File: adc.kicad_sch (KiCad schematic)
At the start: 13 parts, among them U4 PCM1860DBT, U5 STM32F401CDUx, Y1 _ MHz

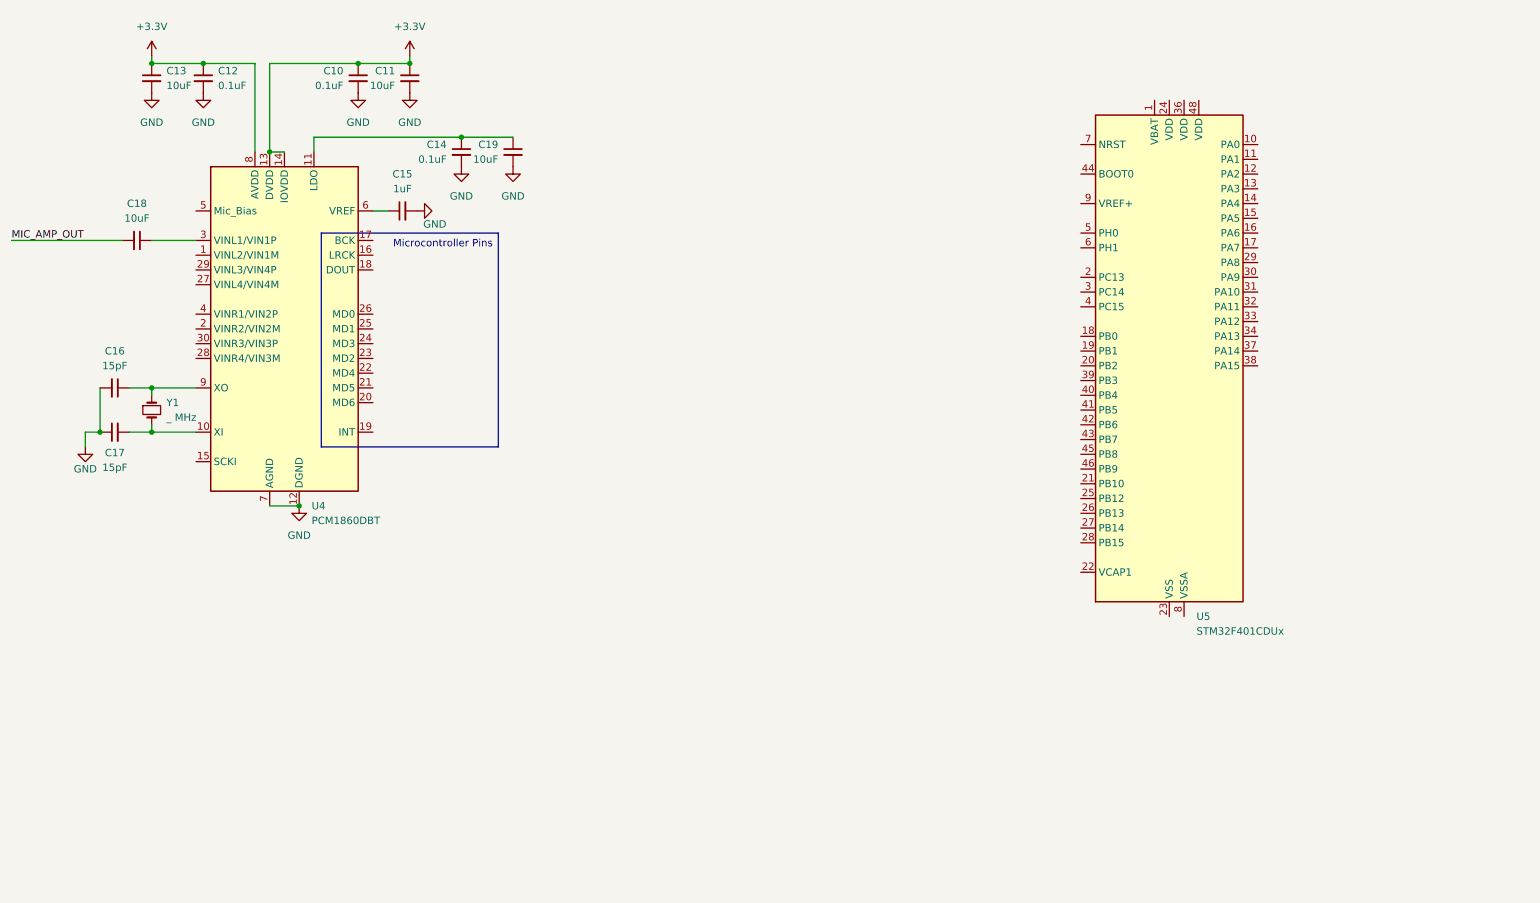
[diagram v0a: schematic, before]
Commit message: implementing full adc and semi-microcontroller
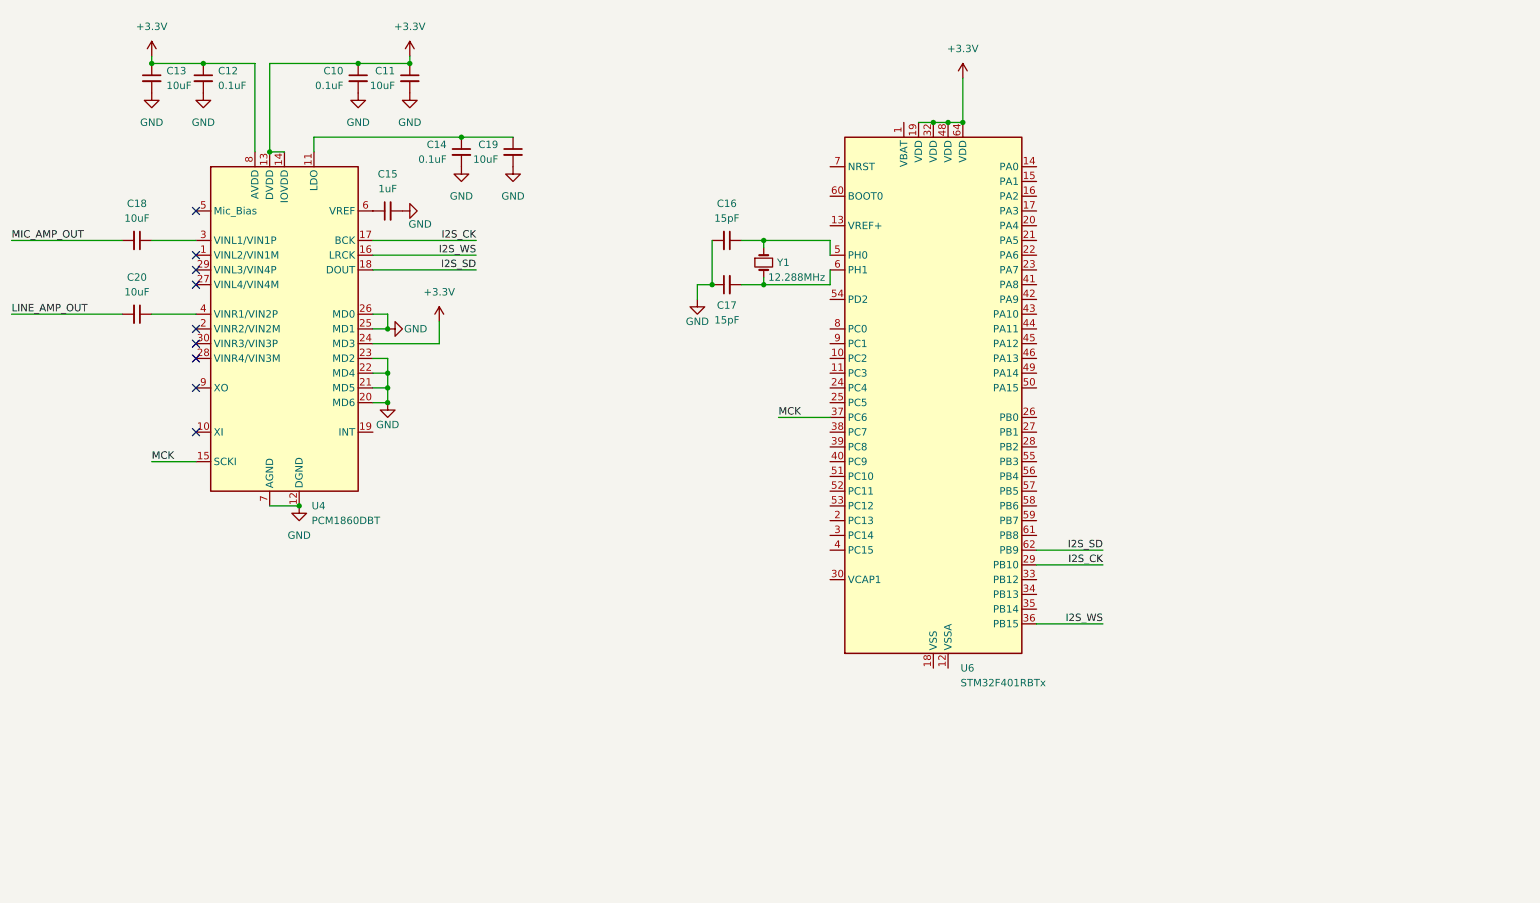
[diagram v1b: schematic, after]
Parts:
- removed U5: STM32F401CDUx, Package_DFN_QFN:QFN-48-1EP_7x7mm_P0.5mm_EP5.6x5.6mm, symbol MCU_ST_STM32F4:STM32F401CDUx
- added C20: 10uF, symbol Device:C_Small
- added U6: STM32F401RBTx, Package_QFP:LQFP-64_10x10mm_P0.5mm, symbol MCU_ST_STM32F4:STM32F401RBTx
- Y1: value _ MHz -> 12.288MHz
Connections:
- net +3.3V: now also U4.24 (MD3), U6.19 (VDD), U6.32 (VDD), U6.48 (VDD), U6.64 (VDD)
- net GND: now also U4.20 (MD6), U4.21 (MD5), U4.22 (MD4), U4.23 (MD2), U4.25 (MD1), U4.26 (MD0)
- net at C16.1, Y1.1: now also U6.5 (PH0); no longer U4.9 (XO)
- net at C17.2, Y1.2: now also U6.6 (PH1); no longer U4.10 (XI)
- net MCK: now reaches U4.15 (SCKI)
- net MCK: now also U6.37 (PC6)
- net I2S_WS: now reaches U4.16 (LRCK)
- net I2S_WS: now also U6.36 (PB15)
- net I2S_CK: now reaches U4.17 (BCK)
- net I2S_CK: now also U6.29 (PB10)
- net I2S_SD: now reaches U4.18 (DOUT)
- net I2S_SD: now also U6.62 (PB9)
- net at U4.4 (VINR1/VIN2P): now also C20.1
- new net: U6.18 (VSS), U6.31 (VSS), U6.47 (VSS), U6.63 (VSS)
- new net LINE_AMP_OUT: C20.2
- no-connect marks 0 -> 9
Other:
- moved on the sheet: C15

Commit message: wow... just wow...
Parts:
- added BOOT: BOOT, symbol Switch:SW_Push
- added C21, C22, C23, C24, C27, C29: 100nF, symbol Device:C_Small
- added C25, C26: 4.7uF, symbol Device:C_Small
- added C28: 1uF, symbol Device:C_Small
- added J4: SWD, Connector:Tag-Connect_TC2030-IDC-NL_2x03_P1.27mm_Vertical, symbol Connector:Conn_ARM_SWD_TagConnect_TC2030-NL
- added R12, R9: 10k, symbol Device:R_Small_US
- added RST: RST, symbol Switch:SW_Push
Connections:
- net +3.3V: now also U6.1 (VBAT), U6.13 (VREF+), BOOT.2, C21.1, C22.1, C23.1, C24.1, C25.1, C27.1, C28.1, J4.1 (VCC)
- net GND: now also U6.12 (VSSA), U6.18 (VSS), U6.31 (VSS), U6.47 (VSS), U6.63 (VSS), C21.2, C22.2, C23.2, C24.2, C25.2, C26.2, C27.2, C28.2, C29.2, J4.5 (GND), R12.2, R9.2, RST.1
- net I2S_SD: now also U6.36 (PB15); no longer U6.62 (PB9)
- net I2S_WS: now also U6.62 (PB9); no longer U6.36 (PB15)
- net at U6.28 (PB2): now also R12.1
- net at U6.30 (VCAP1): now also C26.1
- net SWDIO: now reaches U6.46 (PA13)
- net SWDIO: now also J4.2 (SWDIO)
- net SWCLK: now reaches U6.49 (PA14)
- net SWCLK: now also J4.4 (SWCLK)
- net SWO: now reaches U6.55 (PB3)
- net SWO: now also J4.6 (SWO)
- net BOOT0: now reaches U6.60 (BOOT0)
- net BOOT0: now also BOOT.1, R9.1
- net RST: now reaches U6.7 (NRST)
- net RST: now also C29.1, J4.3 (~{RESET}), RST.2
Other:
- moved on the sheet: C16, C17, C18, C20, U6, Y1

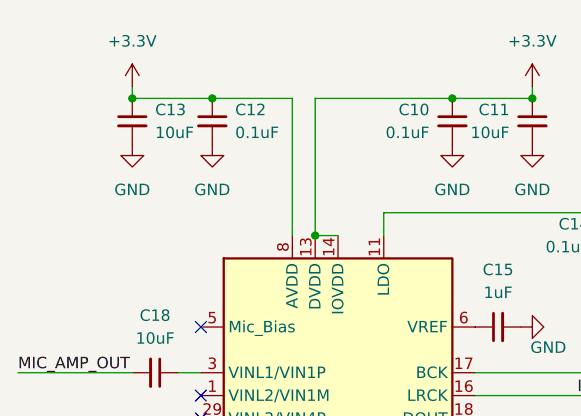
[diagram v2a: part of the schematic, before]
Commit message: Added DAC Page.
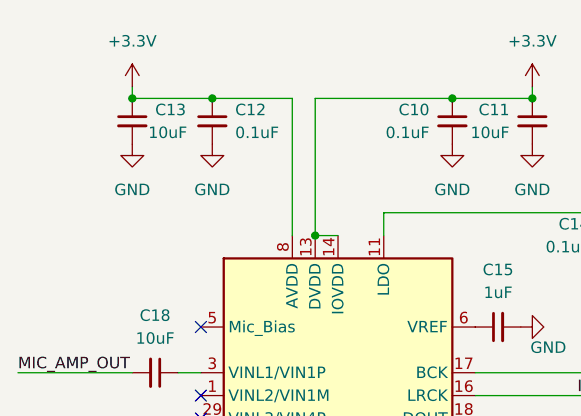
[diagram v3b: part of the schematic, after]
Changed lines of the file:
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@@
 		(in_pos_files yes)
 		(dnp no)
-		(fields_autoplaced yes)
 		(property "Reference" "C13"
 			(at 45.72 24.1362 0)
@@
 		)
 		(property "Value" "10uF"
-			(at 45.72 26.6762 0)
+			(at 44.958 26.67 0)
 			(show_name no)
 			(do_not_autoplace no)
